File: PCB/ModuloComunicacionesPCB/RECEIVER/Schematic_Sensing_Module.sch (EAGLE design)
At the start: 19 parts, among them Q1 MMBT2222A, Q2 MMBT2222A

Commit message: receiver placing
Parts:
- removed U$10: CONN-2.5X5, TERMINAL-TB001:CONN-2.5X5
- removed U$3, U$4, U$7, U$8: TERMINAL-TB2, TERMINAL-TB001:TERMINAL-TB2
- added C4, C5, C6, C7: (no value), rcl:C-EUC1206
- added CARGADOR: MODULO_CARGA_5V, Modulo_Carga:MODULO_CARGA_5V
- added J1: USB3090-XX-X_REVE, USB3090-XX-X_REVE:USB3090-XX-X_REVE
- added JP1: (no value), pinhead:PINHD-1X2
- added JP2: (no value), pinhead:PINHD-1X4
- added REL1, REL2: TERMINAL-TB2, TERMINAL-TB001:TERMINAL-TB2
- added U1, U2: AMS1117-5.0, AMS1117-5.0:AMS1117-5.0
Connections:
- removed net 3V3: C1.1, C2.2, U$9.VCC
- removed net V5+: 1N4007.2, 1N4007SMA.2, U$10.VCC, U$5.VL+, U$6.VL+
- removed net VNEX: C3.1, U$1.VIN, U$8.1
- new net RXNEX: JP2.3, U$1.TX2
- new net TXNEX: JP2.2, U$1.RX2
- new net VBAT: CARGADOR.BAT, CARGADOR.BAT1, JP1.1
- new net VDEVICES: C3.1, C4.1, JP2.4, U$1.VIN, U2.VOUT
- new net VINCHAR: CARGADOR.VIN, CARGADOR.VIN1, J1.VBUS
- new net VOUTCH: C6.1, C7.1, CARGADOR.VOUT, CARGADOR.VOUT1, U1.VIN, U2.VIN
- new net VOUTRELAYS: 1N4007.2, 1N4007SMA.2, C5.1, U$5.VL+, U$6.VL+, U1.VOUT
- new net VXBEE: C1.1, C2.2, U$1.3V3, U$9.VCC
- net CR1: now also REL1.2; no longer U$4.1
- net CR2: now also REL2.2; no longer U$3.1
- net GND: now also C4.2, C5.2, C6.2, C7.2, CARGADOR.GND, CARGADOR.GND1, CARGADOR.GND2, CARGADOR.GND3, CARGADOR.GND4, J1.GND, J1.SHIELD, JP1.2, JP2.1, U$1.GND, U$1.GND1, U1.ADJ/GND, U2.ADJ/GND; no longer U$1.3V3, U$10.GND, U$7.2
- net NOR1: now also REL1.1; no longer U$4.2
- net NOR2: now also REL2.1; no longer U$3.2
- net VR1: now also U$1.D13
- net VR2: now also U$1.D12
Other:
- note added: "ALIMENTACION"
- note added: "BATERIAS"
- note added: "ESP32"
- note added: "PANTALLA"
- note added: "REGULACION"
- note added: "RELAYS"
- note added: "XBEE"
- moved on the sheet: 1N4007, 1N4007SMA, C1, C2, C3, Q1, Q2, R1, R2, U$1, U$5, U$6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

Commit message: screen ino verified screen and placing in receiving corrected
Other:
- note added: "POWER"
- note added: "SCREEN"
- note removed: "ALIMENTACION"
- note removed: "PANTALLA"
- moved on the sheet: C1, C2, C3, C4, C5, C6, C7, CARGADOR, J1, JP1, JP2, U$1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

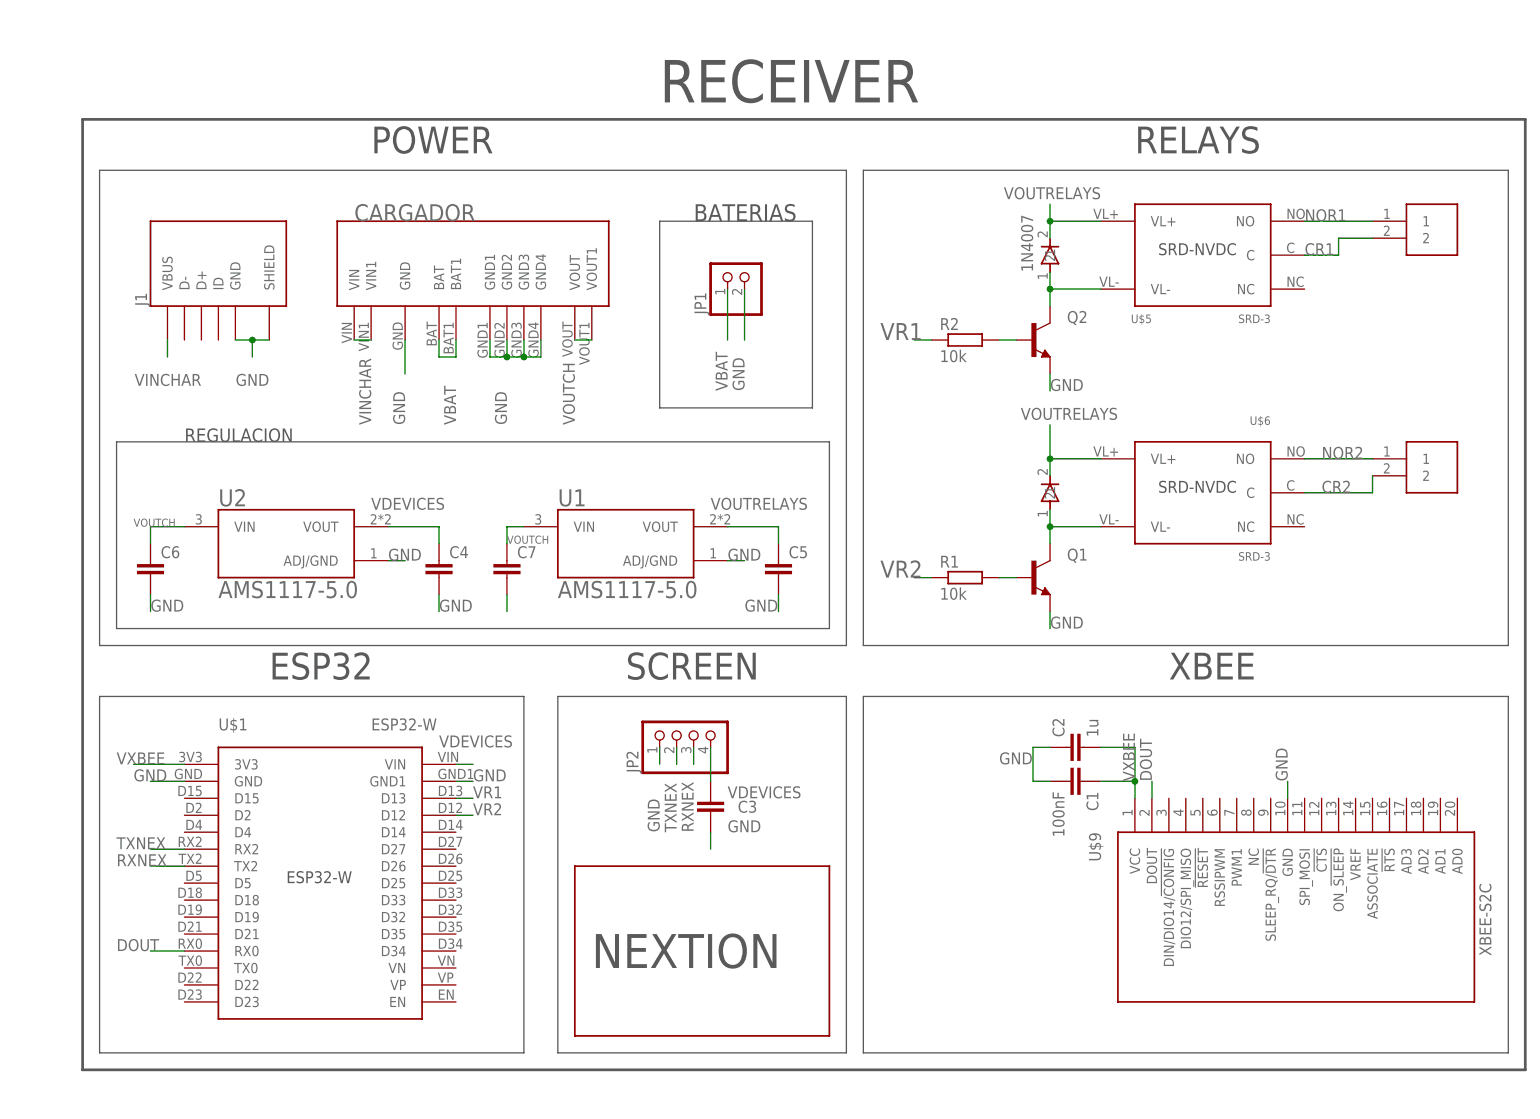
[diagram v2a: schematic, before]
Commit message: pcb enviadas a produccion
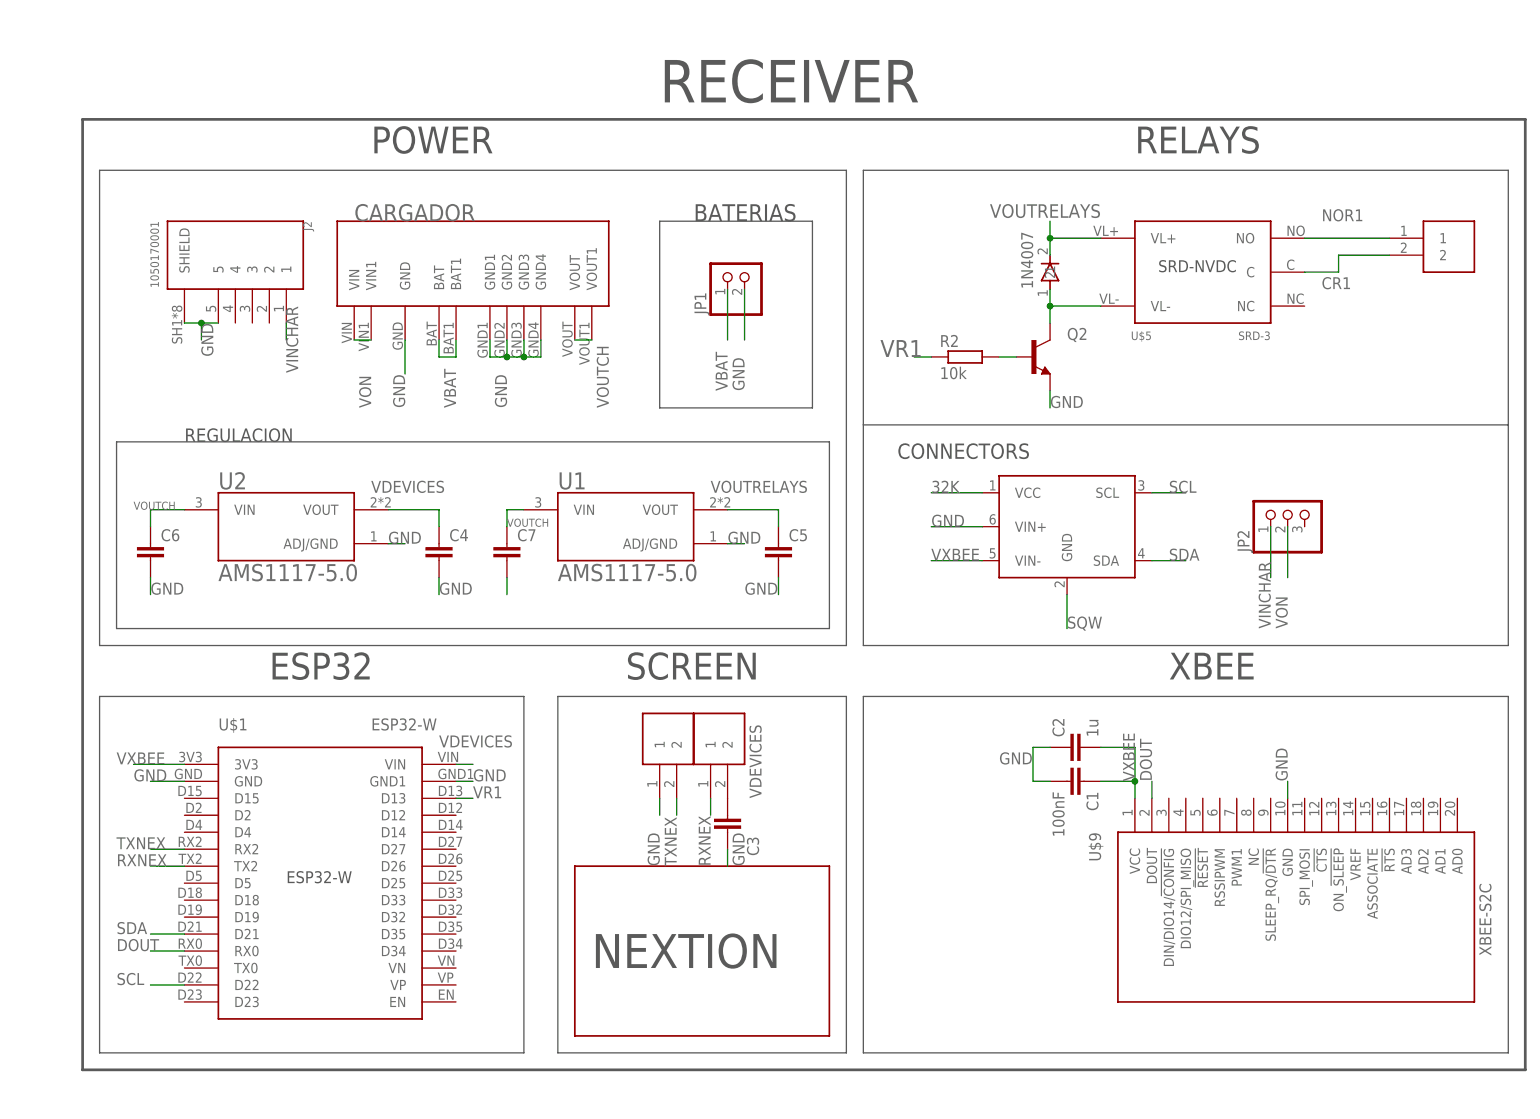
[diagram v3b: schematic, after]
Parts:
- removed 1N4007SMA: 1N4007SMA, 1n400X:1N4007SMA
- removed J1: USB3090-XX-X_REVE, USB3090-XX-X_REVE:USB3090-XX-X_REVE
- removed Q1: MMBT2222A, MMBT2222A:MMBT2222A
- removed R1: 10k, rcl:R-EU_R1206
- removed REL2: TERMINAL-TB2, TERMINAL-TB001:TERMINAL-TB2
- removed U$6: SRD-3, RELE-SRD:SRD-3
- added CONN1, CONN2: TERMINAL-TB2, TERMINAL-TB001:TERMINAL-TB2
- added J2: 1050170001, 1050170001_MOLEX:1050170001
- added U$3: INABB, INA219BB:INABB
- JP2: device pinhead:PINHD-1X4 -> pinhead:PINHD-1X3
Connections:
- removed net CR2: REL2.2, U$6.C
- removed net N$6: 1N4007SMA.1, Q1.C, U$6.VL-
- removed net N$7: Q1.B, R1.2
- removed net NOR2: REL2.1, U$6.NO
- removed net VR2: R1.1, U$1.D12
- new net 32K: U$3.VCC
- new net SCL: U$1.D22, U$3.SCL
- new net SDA: U$1.D21, U$3.SDA
- new net SQW: U$3.GND
- new net VON: CARGADOR.VIN, CARGADOR.VIN1, JP2.2
- net GND: now also CONN1.1, J2.5, J2.SHIELD, U$3.VIN+; no longer J1.GND, J1.SHIELD, JP2.1, Q1.E
- net RXNEX: now also CONN2.1; no longer JP2.3
- net TXNEX: now also CONN1.2; no longer JP2.2
- net VDEVICES: now also CONN2.2; no longer JP2.4
- net VINCHAR: now also J2.1, JP2.1; no longer CARGADOR.VIN, CARGADOR.VIN1, J1.VBUS
- net VOUTRELAYS: no longer 1N4007SMA.2, U$6.VL+
- net VXBEE: now also U$3.VIN-
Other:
- note added: "CONNECTORS"
- moved on the sheet: 1N4007, C3, C4, C5, C6, C7, Q2, R2, U$5, U1, U2
